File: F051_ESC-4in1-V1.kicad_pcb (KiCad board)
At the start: 4 copper layers, 46 x 55.8 mm, 218 parts, among them J1 Conn_01x02, J11 Conn_01x03, J14 Conn_01x03, J2 Conn_01x10, J3 Conn_01x05, J4 Conn_01x05, J5 Conn_01x05, J6 Conn_01x03, J7 Conn_01x05, J8 Conn_01x03, J9 Conn_01x10, Q1 TPHR8504PL, Q10 TPHR8504PL, Q11 TPHR8504PL, Q12 TPHR8504PL, Q13 TPHR8504PL, Q14 TPHR8504PL, Q15 TPHR8504PL, Q16 TPHR8504PL, Q17 TPHR8504PL, Q18 TPHR8504PL, Q19 TPHR8504PL, Q2 TPHR8504PL, Q20 TPHR8504PL, Q21 TPHR8504PL, Q22 TPHR8504PL, Q23 TPHR8504PL, Q24 TPHR8504PL, Q3 TPHR8504PL, Q4 TPHR8504PL, Q5 TPHR8504PL, Q6 TPHR8504PL, Q7 TPHR8504PL, Q8 TPHR8504PL, Q9 TPHR8504PL, U1 STM32F051K6Ux, U10 FD6288Q, U11 STM32F051K6Ux, U12 FD6288Q, U13 L78L12_SOT89, U14 MP4560_QFN10, U2 FD6288Q, U3 L78L12_SOT89, U4 LP2985-3.3, U5 INA139, U6 FD6288Q, U7 OPA340NA, U8 STM32F051K6Ux, U9 STM32F051K6Ux

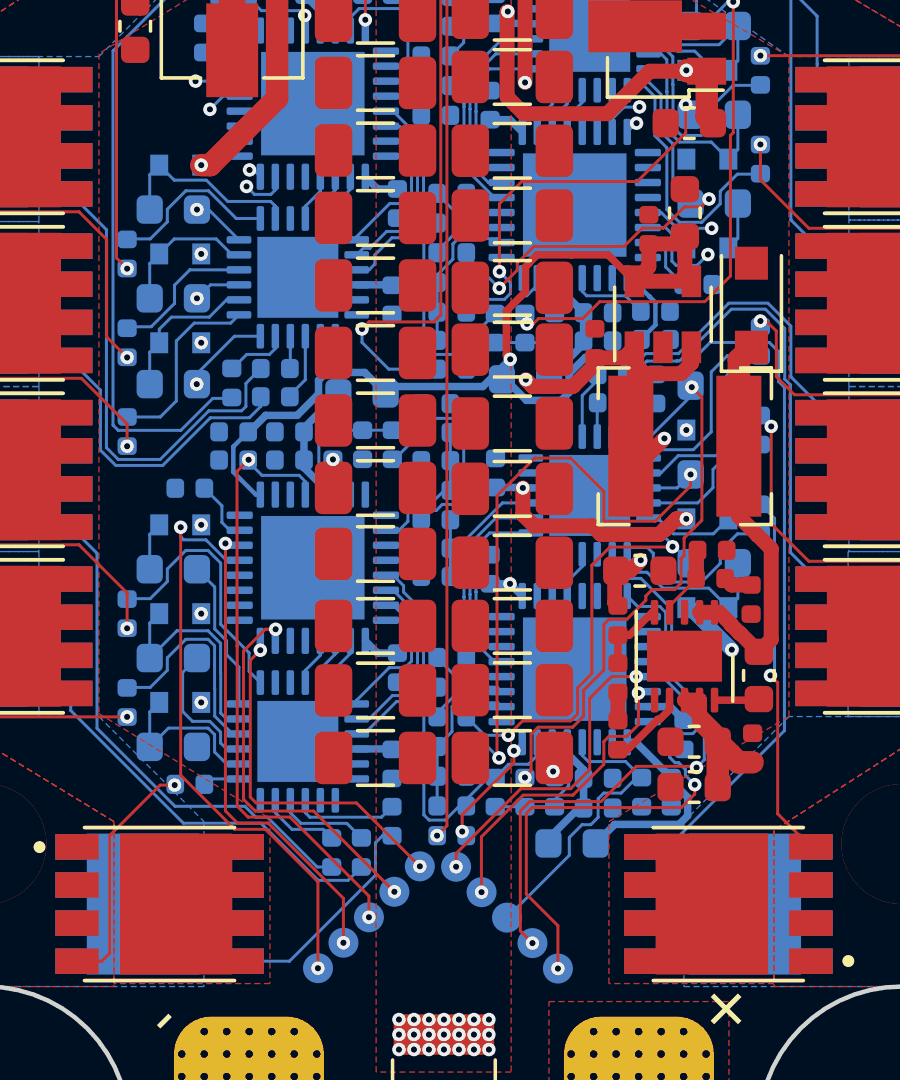
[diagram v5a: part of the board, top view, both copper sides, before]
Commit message: More routing of phase traces
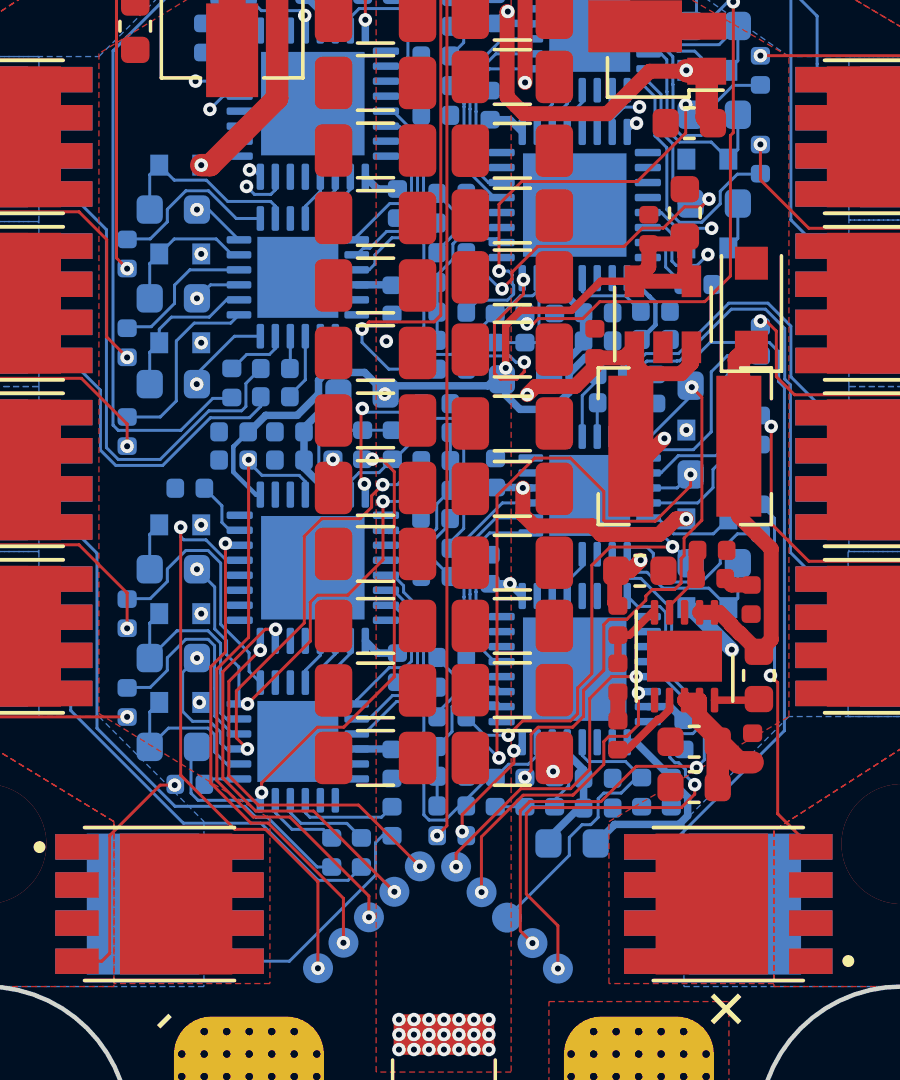
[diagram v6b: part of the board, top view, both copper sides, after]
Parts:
- moved R38 0.99 mm to (139.7, 92.9)
- moved R39 0.95 mm to (139.7, 93.9), turned to 0 degrees
- moved C53 0.35 mm to (142.3, 84.9)
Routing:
- net /MCU 3/PhaseC: track 0.34 -> 18.7 mm, vias 0 -> 2
- net /MCU 3/PhaseB: track 4.59 -> 17.9 mm, vias 0 -> 3
- net /MCU 3/PhaseA: track 5.07 -> 15.8 mm, vias 0 -> 3
- net Net-(R31-Pad1): track 0.00 -> 7.29 mm, vias 0 -> 2
- net Net-(R42-Pad1): track 0.00 -> 5.09 mm, vias 0 -> 2
- net /MCU 2/SenseC: track 2.12 -> 4.67 mm
- net /MCU 3/SenseCOM: track 7.25 -> 9.51 mm
- net /MCU 3/SenseA: track 1.89 -> 4.05 mm
- net +3V3: track 57.6 -> 58.9 mm, vias 2 -> 4
- net /MCU 3/SWCLK: track 12.0 -> 12.6 mm
- net /MCU 3/SWDIO: track 13.0 -> 13.6 mm

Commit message: A lot more traces added
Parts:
- moved U5 65.2 mm to (142.6, 107.0), turned to 270 degrees
- moved U7 64.1 mm to (139.0, 107.0)
- moved J5 2.47 mm to (142.5, 70.8), turned to 45 degrees
- moved FB4 1.55 mm to (135.7, 73.3), turned to 180 degrees
- moved R55 0.99 mm to (139.7, 77.5), turned to 180 degrees
- moved R56 0.99 mm to (139.7, 78.5)
- moved C54 0.20 mm to (142.5, 76.0)
- moved C58 0.20 mm to (142.3, 78.4)
- moved C63 0.10 mm to (137.7, 87.5)
- moved C69 0.05 mm to (136.9, 74.2)
- turned J7 to 315 degrees
- turned R57 to 180 degrees
- turned R58 to 180 degrees
- turned R60 to 270 degrees
- turned R61 to 270 degrees
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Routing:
- net /PWM_3: track 0.00 -> 31.3 mm, vias 0 -> 2
- net /MCU 2/NRST: track 2.67 -> 32.3 mm, vias 0 -> 2
- net /MCU 2/USART1_RX: track 3.20 -> 24.8 mm, vias 1 -> 2
- net /MCU 2/USART1_TX: track 2.35 -> 21.4 mm, vias 1 -> 2
- net /MCU 4/USART1_TX: track 1.17 -> 19.8 mm, vias 1 -> 2
- net /MCU 4/SWDIO: track 1.57 -> 19.6 mm, vias 1 -> 2
- net /MCU 4/SWCLK: track 0.45 -> 18.5 mm, vias 1 -> 2
- net /MCU 4/USART1_RX: track 1.47 -> 18.4 mm, vias 1 -> 2
- net /MCU 4/PhaseC: track 16.9 -> 33.8 mm, vias 1 -> 2
- net /MCU 3/PhaseC: track 18.7 -> 35.0 mm
- net /MCU 1/PhaseA: track 14.4 -> 29.7 mm
- net /MCU 4/PhaseB: track 15.6 -> 30.9 mm, vias 1 -> 2
- net /MCU 3/PhaseA: track 15.8 -> 30.3 mm
- net /MCU 3/PhaseB: track 17.9 -> 32.0 mm
- net /PWM_4: track 0.00 -> 13.1 mm
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
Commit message: Routed a lot more stuff.  Just some more GND and VCC vias to add
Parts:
- added C7: 0.1uF, Capacitor_SMD:C_0402_1005Metric, F.Cu at (143.7, 104.7)
- added C8: 3.3nF, Capacitor_SMD:C_0402_1005Metric, F.Cu at (137.0, 104.2)
- added R2: 60k, Resistor_SMD:R_0402_1005Metric, F.Cu at (141.8, 104.7)
- added R3: 500, Resistor_SMD:R_0402_1005Metric, F.Cu at (138.4, 104.7)
- moved R23 1.41 mm to (149.2, 87.2), turned to 180 degrees
- moved R70 1.23 mm to (130.6, 89.7), turned to 0 degrees
- moved R77 0.25 mm to (150.2, 95.4)
- moved U5 0.13 mm to (142.7, 106.9), turned to 0 degrees
- moved R18 0.10 mm to (150.4, 92.9)
- moved R20 0.10 mm to (150.4, 90.0)
- moved R66 0.10 mm to (129.5, 84.1)
- moved R68 0.10 mm to (129.5, 87.0)
- moved R4 0.09 mm to (150.5, 80.9)
- moved R49 0.09 mm to (129.5, 96.1)
- moved R51 0.09 mm to (129.5, 99.0)
- moved R6 0.09 mm to (150.5, 78.0)
- moved C16 0.08 mm to (137.7, 101.0)
- moved Q15 0.06 mm to (124.8, 96.9)
- moved Q16 0.06 mm to (124.8, 96.9)
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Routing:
- net /Curent Sense/CURR: track 0.00 -> 45.3 mm, vias 0 -> 3
- net +3V3: track 55.0 -> 70.6 mm, vias 4 -> 7
- net +12V: track 47.5 -> 58.1 mm, vias 13 -> 16
- net VCC_Shunt: track 12.9 -> 21.6 mm, vias 21 -> 151
- net Net-(R3-Pad2): track 0.00 -> 7.44 mm
- net GND: track 0.95 -> 8.15 mm, vias 60 -> 141
- net VCC: track 0.00 -> 7.09 mm
- net Net-(R2-Pad1): track 0.00 -> 5.01 mm
- net /PWM_3: track 31.3 -> 34.2 mm, vias 2 -> 3
- net Net-(Q20-Pad4): track 23.0 -> 20.1 mm, vias 0 -> 2
- net Net-(Q3-Pad4): track 11.6 -> 14.3 mm
- net Net-(Q15-Pad4): track 7.71 -> 10.4 mm
- net /MCU 3/SWDIO: track 14.8 -> 17.4 mm
- net /MCU 4/PhaseA: track 28.6 -> 30.7 mm, vias 2 -> 11
- net /PWM_4: track 13.1 -> 14.9 mm, vias 0 -> 1
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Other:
- board text removed: "Think about flipping the sense “rows”(3). Might make routing the phases easier"
